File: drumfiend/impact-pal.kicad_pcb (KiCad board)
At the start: 2 copper layers, 160.6 x 128.5 mm, 217 parts, among them J1 AudioJack2, J10 AudioJack2, J11 AudioJack2, J12 AudioJack2, J13 AudioJack2, J14 AudioJack2, J15 AudioJack2, J16 AudioJack2, J17 AudioJack2, J18 AudioJack2, J19 AudioJack2, J2 AudioJack2, J20 AudioJack3, J21 Conn_01x03_Male, J22 Conn_01x03_Male, J23 Conn_02x05_Odd_Even, J24 Conn_01x10_Male, J25 Conn_01x10_Male, J26 Conn_01x10_Male, J27 Conn_01x10_Male, J28 Conn_01x04_Male, J29 Conn_01x04_Male, J3 AudioJack2, J30 Conn_01x04_Male, J31 Conn_01x04_Male, J4 AudioJack2, J5 AudioJack2, J6 AudioJack2, J7 AudioJack2, J8 AudioJack2, J9 AudioJack2, Q1 MMBT3904, Q10 MMBT3904, Q11 MMBT3904, Q12 MMBT3904, Q13 MMBT3904, Q14 MMBT3904, Q15 MMBT3904, Q16 MMBT3904, Q17 MMBT3904, Q18 MMBT3904, Q19 MMBT3904, Q2 MMBT3904, Q3 MMBT3904, Q4 MMBT3904, Q5 MMBT3904, Q6 MMBT3904, Q7 MMBT3904, Q8 MMBT3904, Q9 MMBT3904, U1 L78L05_TO92, U2 Teensy3.2

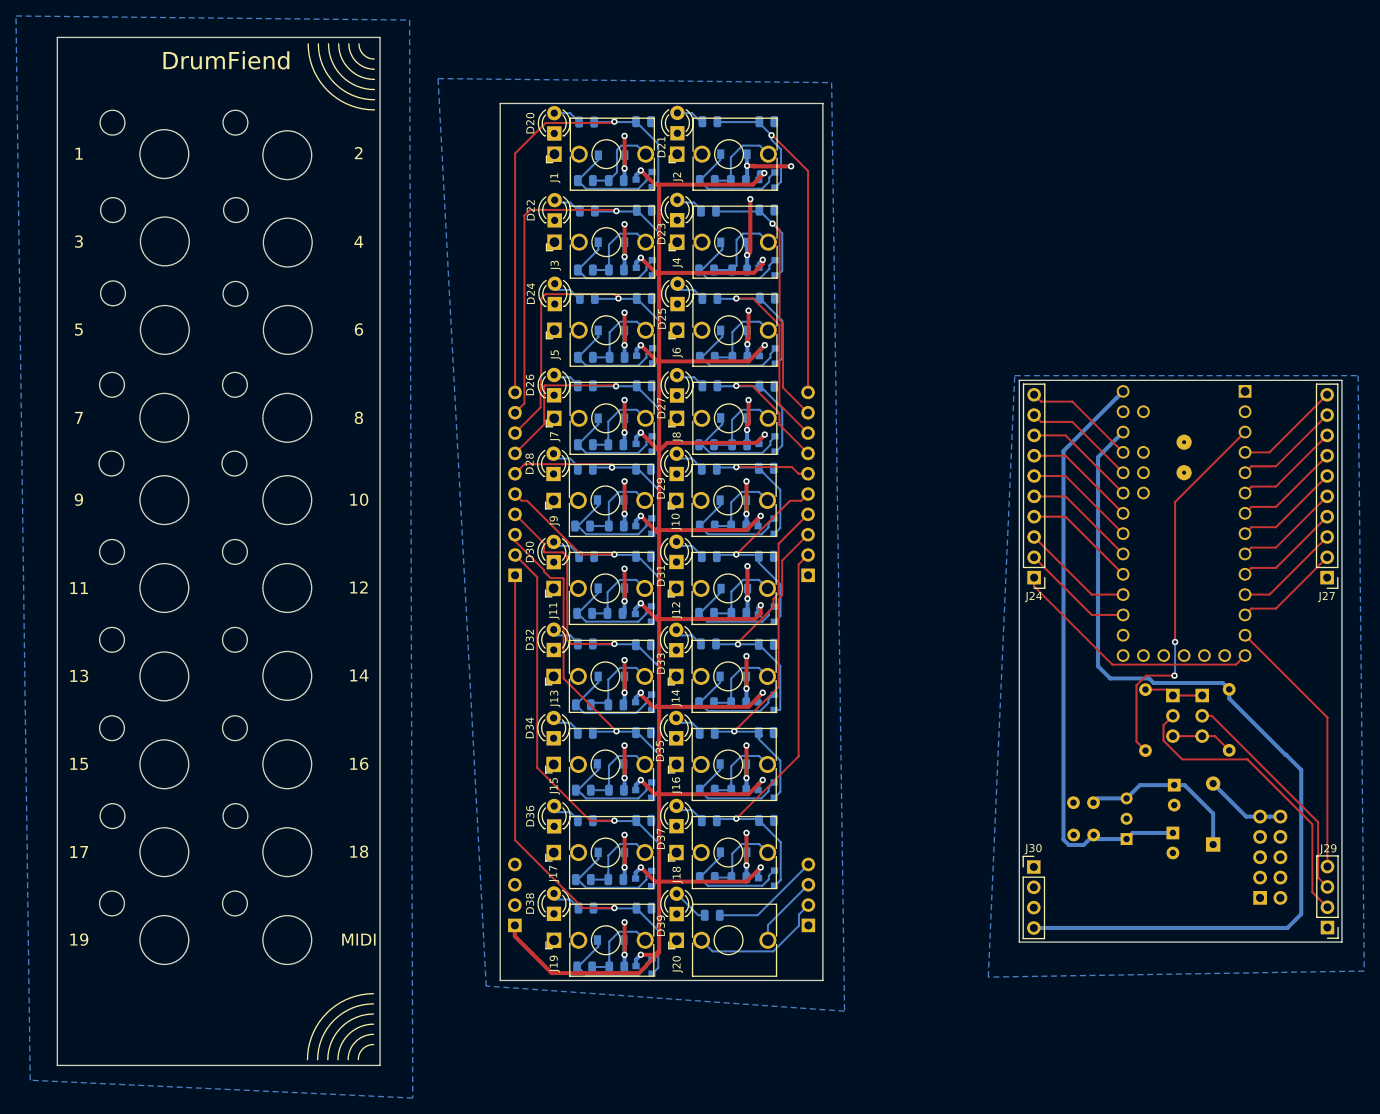
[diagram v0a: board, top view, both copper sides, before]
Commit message: Updating schematic, project, PCB for drumfiend
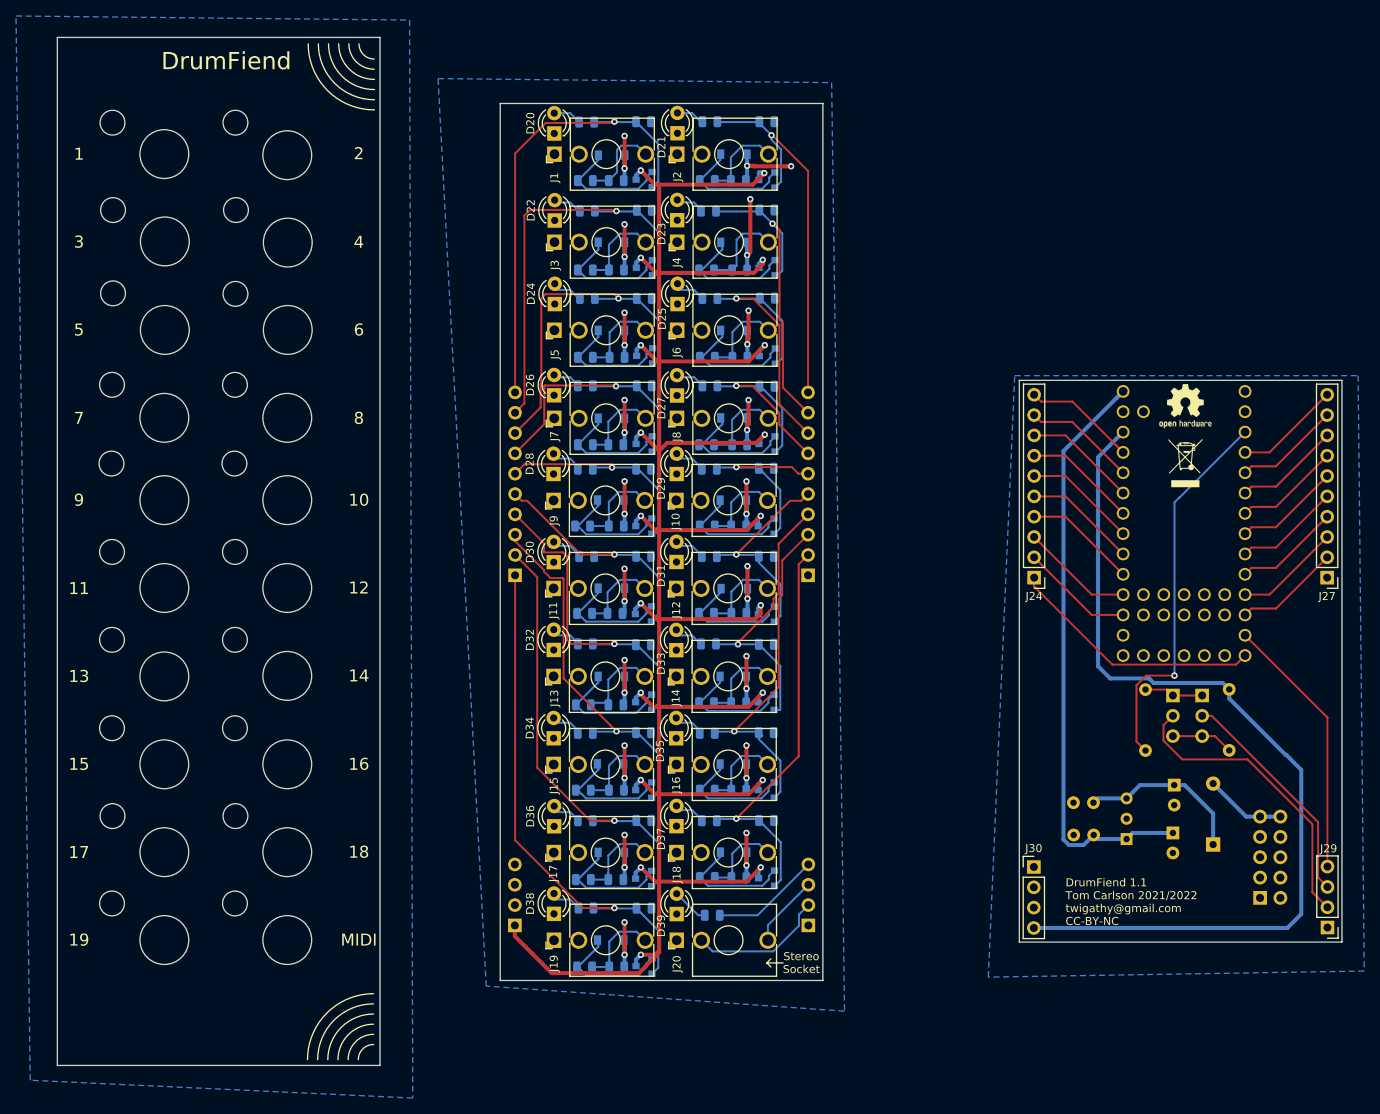
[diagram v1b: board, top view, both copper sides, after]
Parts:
- added REF**: WEEE-Logo_4.2x6mm_SilkScreen, Symbol:WEEE-Logo_4.2x6mm_SilkScreen, F.Cu at (102.9, 61.2)
- added REF**: OSHW-Logo2_7.3x6mm_SilkScreen, Symbol:OSHW-Logo2_7.3x6mm_SilkScreen, F.Cu at (102.9, 54.1)
- added REF**: WEEE-Logo_4.2x6mm_SilkScreen, Symbol:WEEE-Logo_4.2x6mm_SilkScreen, B.Cu at (-1.78, 12.4)
- added REF**: OSHW-Logo2_7.3x6mm_SilkScreen, Symbol:OSHW-Logo2_7.3x6mm_SilkScreen, B.Cu at (-1.78, 19.6)
- added REF**: WEEE-Logo_4.2x6mm_SilkScreen, Symbol:WEEE-Logo_4.2x6mm_SilkScreen, B.Cu at (19.8, 25.7)
- added REF**: OSHW-Logo2_7.3x6mm_SilkScreen, Symbol:OSHW-Logo2_7.3x6mm_SilkScreen, B.Cu at (54.1, 26.2)
- U2: footprint RS:Teensy30_31_32_LC -> Divergent:Teensy40
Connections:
- J23 pad 1: Net-(J23-Pad1) -> unconnected-(J23-Pad1)
- J23 pad 2: Net-(J23-Pad2) -> unconnected-(J23-Pad2)
- U2 pad 15: Net-(U2-Pad15) -> unconnected-(U2-Pad15)
- U2 pad 16: Net-(U2-Pad16) -> unconnected-(U2-Pad16)
- U2 pad 18: Net-(U2-Pad18) -> unconnected-(U2-Pad18)
- U2 pad 19: Net-(U2-Pad19) -> unconnected-(U2-Pad19)
- U2 pad 2: Net-(U2-Pad2) -> unconnected-(U2-Pad2)
- U2 pad 20: Net-(U2-Pad20) -> unconnected-(U2-Pad20)
- U2 pad 21: Net-(U2-Pad21) -> unconnected-(U2-Pad21)
- U2 pad 34: Net-(U2-Pad34) -> unconnected-(U2-Pad34)
- U2 pad 35: Net-(U2-Pad35) -> unconnected-(U2-Pad35)
- U2 pad 36: Net-(U2-Pad36) -> unconnected-(U2-Pad36)
- U2 pad 37: Net-(U2-Pad37) -> unconnected-(U2-Pad37)
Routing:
- net Net-(R79-Pad1): vias 2 -> 1
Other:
- net class Default removed
- net class Power removed
- board text added: "DrumFiend 1.1 Tom Carlson 2021/2022 twigathy@gmail.com CC-BY-NC"
- board text added: "Stereo Socket"
- board text added: "Teensy 4.0"
- board text added: "USB"
- board text removed: "Teensy 3.2"
